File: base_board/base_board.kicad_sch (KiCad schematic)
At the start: 54 parts, among them J1 Conn_ARM_JTAG_SWD_20, J2 Conn_01x20_Pin, J3 Conn_01x20_Socket, SW1 SW_Push, U1 STM32F446ZEJx, U2 IS42S16400J-xT, U3 BMI270, U4 USB_C_Receptacle_USB2.0, U5 10p, U6 10p, U7 LD3985M33R_SOT23, Y1 Crystal_GND24

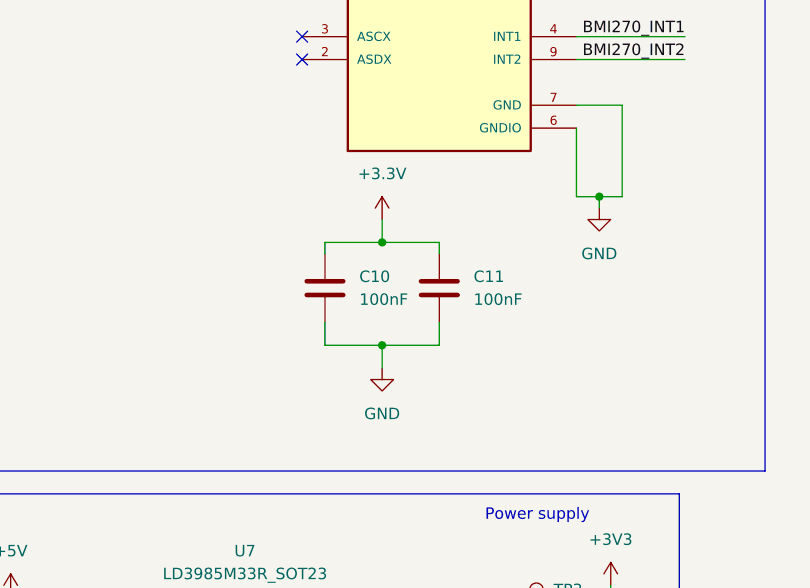
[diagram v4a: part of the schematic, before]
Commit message: [pcb] added route for BMI270
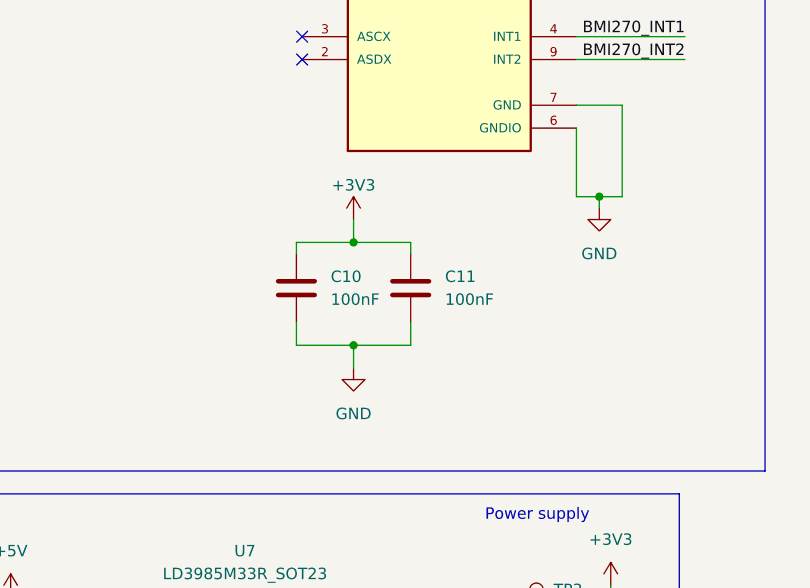
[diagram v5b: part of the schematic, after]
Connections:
- net +3.3V: no longer C10.2, C11.2
- net +3V3: now also C10.2, C11.2
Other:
- moved on the sheet: C10, C11
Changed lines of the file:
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@@
   (junction (at 163.83 19.685) (diameter 0) (color 0 0 0 0)
   )
-  (junction (at 67.945 173.99) (diameter 0) (color 0 0 0 0)
+  (junction (at 64.77 173.99) (diameter 0) (color 0 0 0 0)
   )
   (junction (at 176.53 209.55) (diameter 0) (color 0 0 0 0)
@@
   (junction (at 175.26 209.55) (diameter 0) (color 0 0 0 0)
   )
-  (junction (at 67.945 185.42) (diameter 0) (color 0 0 0 0)
+  (junction (at 64.77 185.42) (diameter 0) (color 0 0 0 0)
   )
   (junction (at 339.09 228.6) (diameter 0) (color 0 0 0 0)
@@
     (stroke (width 0) (type default))
   )
-  (wire (pts (xy 67.945 171.45) (xy 67.945 173.99))
+  (wire (pts (xy 64.77 171.45) (xy 64.77 173.99))
     (stroke (width 0) (type default))
   )
@@
     (stroke (width 0) (type default))
   )
-  (wire (pts (xy 61.595 173.99) (xy 67.945 173.99))
+  (wire (pts (xy 58.42 173.99) (xy 64.77 173.99))
     (stroke (width 0) (type default))
   )
@@
     (stroke (width 0) (type default))
   )
-  (wire (pts (xy 74.295 173.99) (xy 74.295 175.26))
+  (wire (pts (xy 71.12 173.99) (xy 71.12 175.26))
     (stroke (width 0) (type default))
   )
@@
     (stroke (width 0) (type default))
   )
-  (wire (pts (xy 67.945 185.42) (xy 67.945 187.96))
+  (wire (pts (xy 64.77 185.42) (xy 64.77 187.96))
     (stroke (width 0) (type default))
   )
@@
     (stroke (width 0) (type default))
   )
-  (wire (pts (xy 67.945 185.42) (xy 74.295 185.42))
+  (wire (pts (xy 64.77 185.42) (xy 71.12 185.42))
     (stroke (width 0) (type default))
   )
@@
     (stroke (width 0) (type default))
   )
-  (wire (pts (xy 61.595 175.26) (xy 61.595 173.99))
+  (wire (pts (xy 58.42 175.26) (xy 58.42 173.99))
     (stroke (width 0) (type default))
   )
@@
     (stroke (width 0) (type default))
   )
-  (wire (pts (xy 61.595 182.88) (xy 61.595 185.42))
+  (wire (pts (xy 58.42 182.88) (xy 58.42 185.42))
     (stroke (width 0) (type default))
   )
@@
     (stroke (width 0) (type default))
   )
-  (wire (pts (xy 74.295 185.42) (xy 74.295 182.88))
+  (wire (pts (xy 71.12 185.42) (xy 71.12 182.88))
     (stroke (width 0) (type default))
   )
@@
     (stroke (width 0) (type default))
   )
-  (wire (pts (xy 67.945 173.99) (xy 74.295 173.99))
+  (wire (pts (xy 64.77 173.99) (xy 71.12 173.99))
     (stroke (width 0) (type default))
   )
@@
     (stroke (width 0) (type default))
   )
-  (wire (pts (xy 61.595 185.42) (xy 67.945 185.42))
+  (wire (pts (xy 58.42 185.42) (xy 64.77 185.42))
     (stroke (width 0) (type default))
   )
@@
     )
   )
-  (symbol (lib_id "power:+3.3V") (at 67.945 171.45 0) (unit 1)
-    (in_bom yes) (on_board yes) (dnp no) (fields_autoplaced)
-    (property "Reference" "#PWR0106" (at 67.945 175.26 0)
-      (effects (font (size 1.27 1.27)) hide)
-    )
-    (property "Value" "+3.3V" (at 67.945 166.37 0)
-      (effects (font (size 1.27 1.27)))
-    )
-    (property "Footprint" "" (at 67.945 171.45 0)
-      (effects (font (size 1.27 1.27)) hide)
-    )
-    (property "Datasheet" "" (at 67.945 171.45 0)
-      (effects (font (size 1.27 1.27)) hide)
-    )
-    (pin "1")
-    (instances
-      (project "base_board"
-        (path "/2307506f-1d7e-4fdb-b101-b9905788fe29"
-          (reference "#PWR0106") (unit 1)
-        )
-      )
-    )
-  )
   (symbol (lib_id "Device:C") (at 271.78 154.94 0) (unit 1)
     (in_bom yes) (on_board yes) (dnp no) (fields_autoplaced)
@@
     )
   )
+  (symbol (lib_name "+3V3_1") (lib_id "power:+3V3") (at 64.77 171.45 0) (unit 1)
+    (in_bom yes) (on_board yes) (dnp no) (fields_autoplaced)
+    (property "Reference" "#PWR01" (at 64.77 175.26 0)
+      (effects (font (size 1.27 1.27)) hide)
+    )
+    (property "Value" "+3V3" (at 64.77 167.64 0)
+      (effects (font (size 1.27 1.27)))
+    )
+    (property "Footprint" "" (at 64.77 171.45 0)
+      (effects (font (size 1.27 1.27)) hide)
+    )
+    (property "Datasheet" "" (at 64.77 171.45 0)
+      (effects (font (size 1.27 1.27)) hide)
+    )
+    (pin "1")
+    (instances
+      (project "base_board"
+        (path "/2307506f-1d7e-4fdb-b101-b9905788fe29"
+          (reference "#PWR01") (unit 1)
+        )
+      )
+    )
+  )
   (symbol (lib_id "power:GND") (at 287.02 127 0) (unit 1)
     (in_bom yes) (on_board yes) (dnp no) (fields_autoplaced)
@@
     )
   )
-  (symbol (lib_id "power:GND") (at 67.945 187.96 0) (unit 1)
+  (symbol (lib_id "power:GND") (at 64.77 187.96 0) (unit 1)
     (in_bom yes) (on_board yes) (dnp no) (fields_autoplaced)
-    (property "Reference" "#PWR0108" (at 67.945 194.31 0)
+    (property "Reference" "#PWR0108" (at 64.77 194.31 0)
       (effects (font (size 1.27 1.27)) hide)
     )
-    (property "Value" "GND" (at 67.945 193.04 0)
+    (property "Value" "GND" (at 64.77 193.04 0)
       (effects (font (size 1.27 1.27)))
     )
-    (property "Footprint" "" (at 67.945 187.96 0)
+    (property "Footprint" "" (at 64.77 187.96 0)
       (effects (font (size 1.27 1.27)) hide)
     )
-    (property "Datasheet" "" (at 67.945 187.96 0)
+    (property "Datasheet" "" (at 64.77 187.96 0)
       (effects (font (size 1.27 1.27)) hide)
     )
@@
     )
   )
-  (symbol (lib_id "Device:C") (at 74.295 179.07 180) (unit 1)
+  (symbol (lib_id "Device:C") (at 71.12 179.07 180) (unit 1)
     (in_bom yes) (on_board yes) (dnp no) (fields_autoplaced)
-    (property "Reference" "C11" (at 78.105 177.7999 0)
+    (property "Reference" "C11" (at 74.93 177.7999 0)
       (effects (font (size 1.27 1.27)) (justify right))
     )
-    (property "Value" "100nF" (at 78.105 180.3399 0)
+    (property "Value" "100nF" (at 74.93 180.3399 0)
       (effects (font (size 1.27 1.27)) (justify right))
     )
-    (property "Footprint" "Capacitor_SMD:C_0603_1608Metric" (at 73.3298 175.26 0)
+    (property "Footprint" "Capacitor_SMD:C_0603_1608Metric" (at 70.1548 175.26 0)
       (effects (font (size 1.27 1.27)) hide)
     )
-    (property "Datasheet" "~" (at 74.295 179.07 0)
+    (property "Datasheet" "~" (at 71.12 179.07 0)
       (effects (font (size 1.27 1.27)) hide)
     )
@@
     )
   )
-  (symbol (lib_id "Device:C") (at 61.595 179.07 180) (unit 1)
+  (symbol (lib_id "Device:C") (at 58.42 179.07 180) (unit 1)
     (in_bom yes) (on_board yes) (dnp no) (fields_autoplaced)
-    (property "Reference" "C10" (at 65.405 177.7999 0)
+    (property "Reference" "C10" (at 62.23 177.7999 0)
       (effects (font (size 1.27 1.27)) (justify right))
     )
-    (property "Value" "100nF" (at 65.405 180.3399 0)
+    (property "Value" "100nF" (at 62.23 180.3399 0)
       (effects (font (size 1.27 1.27)) (justify right))
     )
-    (property "Footprint" "Capacitor_SMD:C_0603_1608Metric" (at 60.6298 175.26 0)
+    (property "Footprint" "Capacitor_SMD:C_0603_1608Metric" (at 57.4548 175.26 0)
       (effects (font (size 1.27 1.27)) hide)
     )
-    (property "Datasheet" "~" (at 61.595 179.07 0)
+    (property "Datasheet" "~" (at 58.42 179.07 0)
       (effects (font (size 1.27 1.27)) hide)
     )

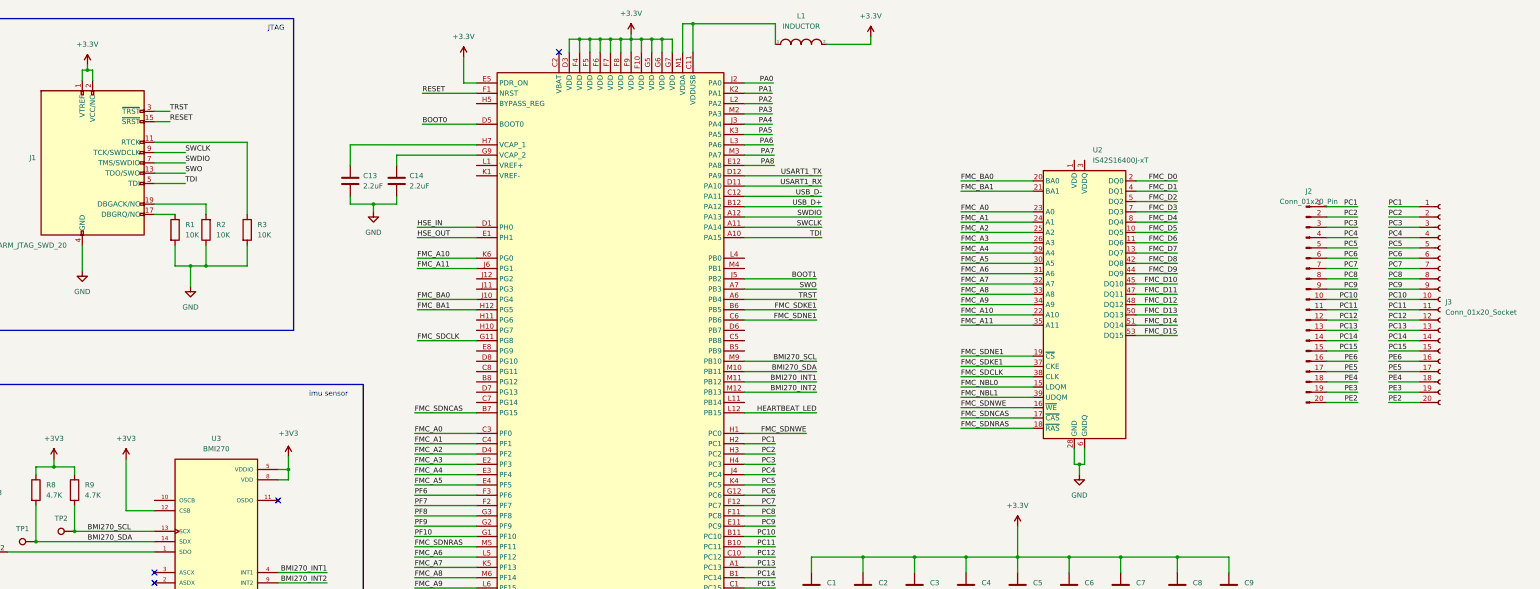
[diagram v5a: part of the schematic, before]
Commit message: [pcb] completed sdram routing
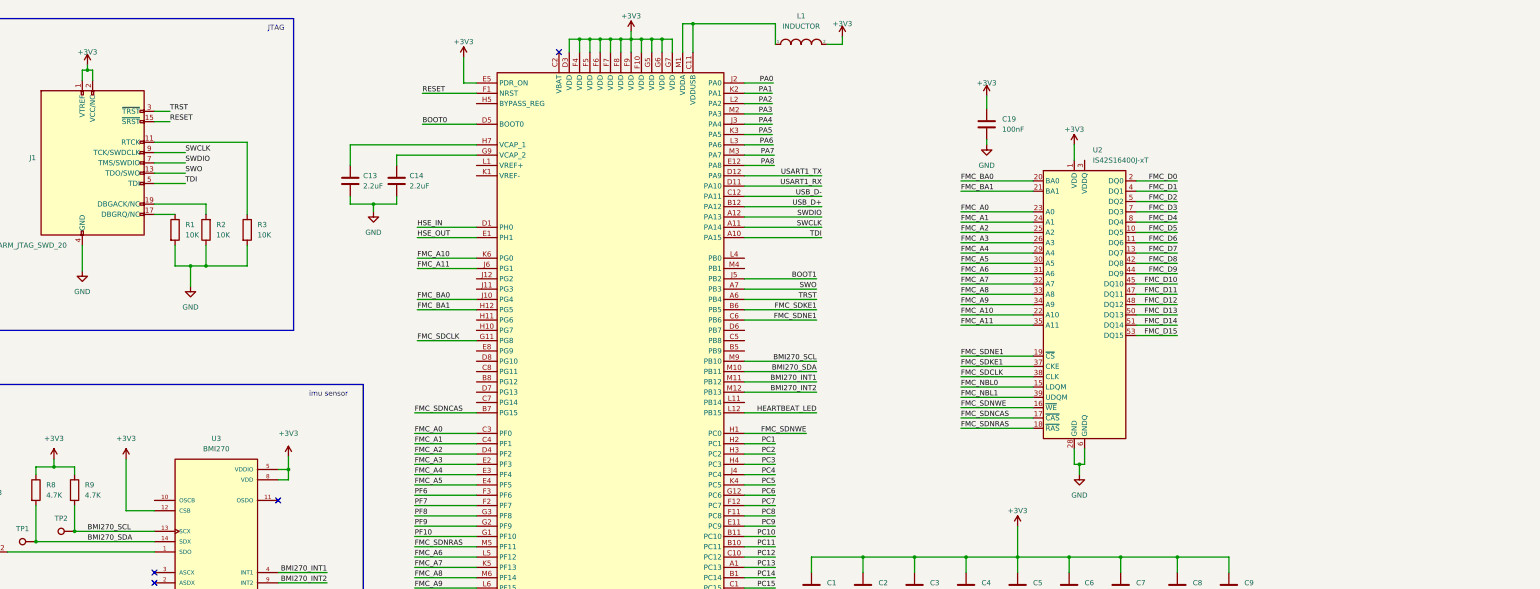
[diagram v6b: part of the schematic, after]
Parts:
- removed J2: Conn_01x20_Pin, Connector_PinHeader_2.54mm:PinHeader_1x20_P2.54mm_Vertical, symbol Connector:Conn_01x20_Pin
- removed J3: Conn_01x20_Socket, Connector_PinSocket_2.54mm:PinSocket_1x20_P2.54mm_Vertical, symbol Connector:Conn_01x20_Socket
- added C19: 100nF, Capacitor_SMD:C_0603_1608Metric, symbol Device:C
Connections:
- net +3.3V: no longer C1.1, C2.1, C3.1, C4.1, C5.1, C6.1, C7.1, C8.1, C9.1, L1.2, U1.D3 (VDD), U1.E5 (PDR_ON), U1.F10 (VDD), U1.F4 (VDD), U1.F5 (VDD), U1.F6 (VDD), U1.F7 (VDD), U1.F8 (VDD), U1.F9 (VDD), U1.G5 (VDD), U1.G6 (VDD), U1.G7 (VDD)
- net +3V3: now also C1.1, C2.1, C3.1, C4.1, C5.1, C6.1, C7.1, C8.1, C9.1, L1.2, U1.D3 (VDD), U1.E5 (PDR_ON), U1.F10 (VDD), U1.F4 (VDD), U1.F5 (VDD), U1.F6 (VDD), U1.F7 (VDD), U1.F8 (VDD), U1.F9 (VDD), U1.G5 (VDD), U1.G6 (VDD), U1.G7 (VDD), U2.1 (VDD), U2.14 (VDD), U2.27 (VDD), C19.1
- net GND: now also C19.2
